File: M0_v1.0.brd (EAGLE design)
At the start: 68.6 x 53.3 mm, 54 parts, among them CN1 POWER_JACK, CN2 47346-0001, CN3 DIGITAL10, CN4 DIGITAL8, CN5 ICSP, CN6 POWER8, CN7 ANALOG6, IC1 AMS1117-5.0, IC2 AMS1117-3.3, IC3 MCP6002T-I/SN, Q2 16MHz, T1 AO3401A, T2 2N7002, U1 ATSAMD21G-A

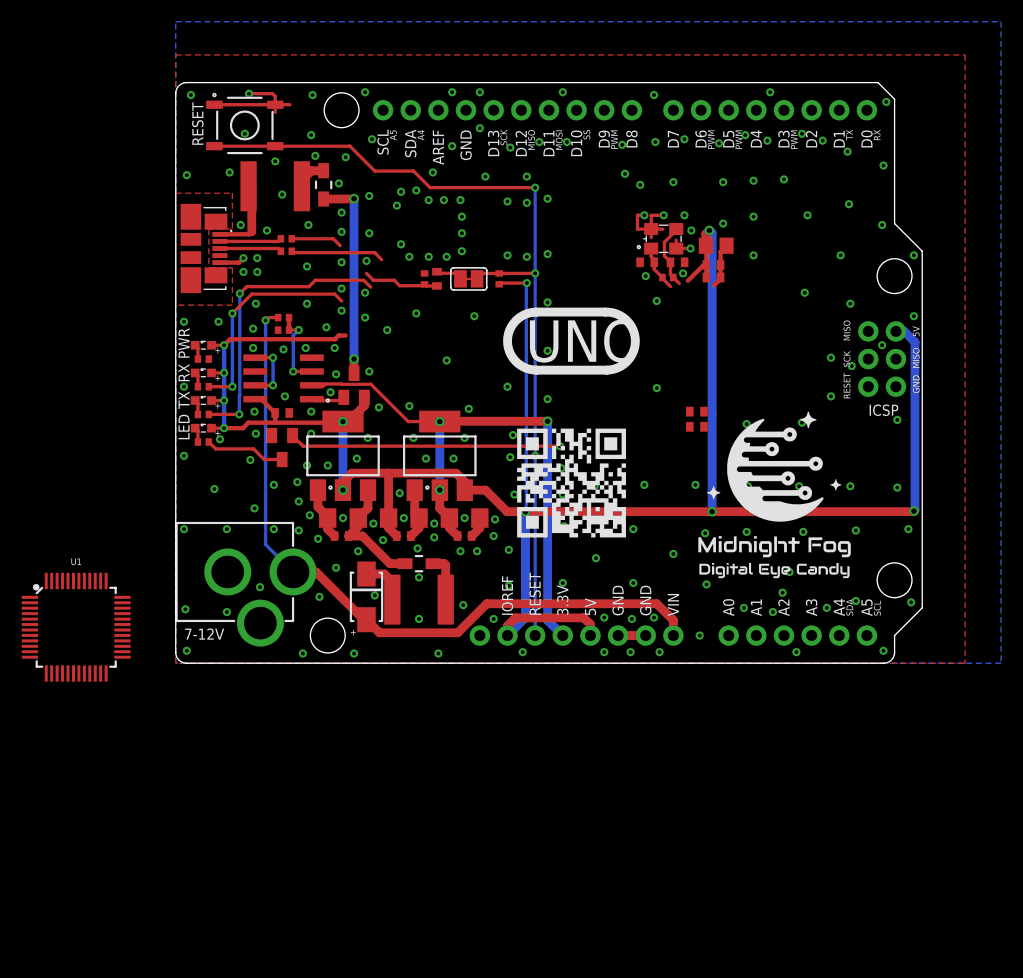
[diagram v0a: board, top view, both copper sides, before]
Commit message: Add basic signal wiring.
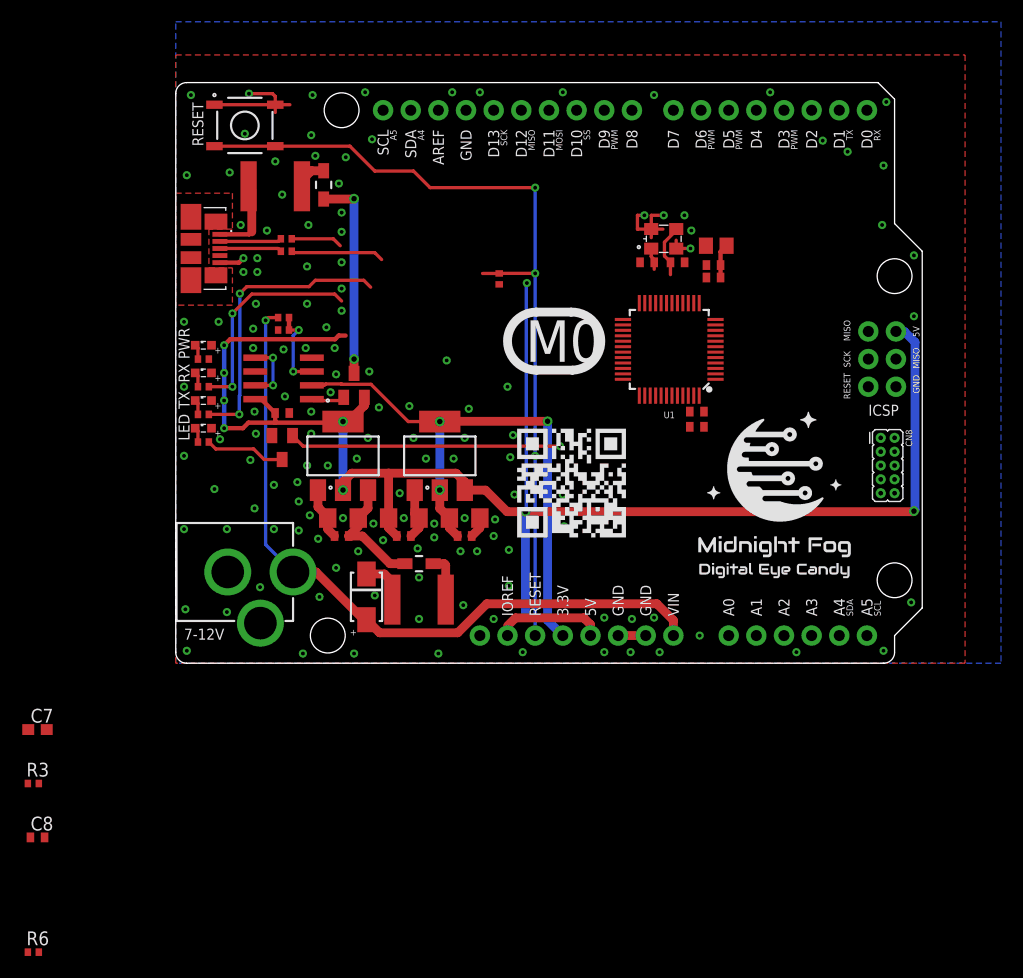
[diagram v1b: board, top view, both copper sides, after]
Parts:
- removed C18: 100nF, rcl:C0402
- removed R11: 1K, rcl:R0402
- removed SJ1: USB_RESET, _my_jumpers:SJ
- added C7: 1uF, rcl:C0603
- added C8: 10nF, rcl:C0402
- added CN8: SWD, SparkFun-Connectors:2X5_PTH_SILK_.05
- added R3: 330R, rcl:R0402
- Q2: value 16MHz -> 32.768KHz
- R10, R7, R8, R9: value 1K -> 470R
- R6: value 1M -> 330R
- U1: value ATSAMD21G-A -> ATSAMD21G-AU
- moved R6 85.1 mm to (-13.1, -26.5)
- moved U1 60.2 mm to (45.3, 28.8), turned to 180 degrees
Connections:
- removed net A4_SDA: CN3.2, CN7.2
- removed net A5_SCL: CN3.1, CN7.1
- removed net MCU_OSC_IN: C12.2, Q2.3, R6.2
- removed net MCU_OSC_OUT: C13.2, Q2.1, R6.1
- removed net N$5: C18.2, SJ1.1
- removed net USB_DTR: C18.1, R11.2
- new net A4: CN7.2, U1.10
- new net A5: CN7.1, U1.47
- new net MCU_OSC32_IN: C12.2, Q2.3, U1.1
- new net MCU_OSC32_OUT: C13.2, Q2.1, U1.2
- new net MCU_RESET: C8.1, R3.1, U1.40
- new net N$20: U1.48
- new net N$28: U1.22
- new net N$41: U1.39
- new net N$47: U1.37
- new net N$48: U1.38
- new net N$6: U1.4
- new net SCL: CN3.1, U1.32
- new net SDA: CN3.2, U1.31
- new net SPI_MISO: CN5.1, U1.21
- new net SPI_MOSI: CN5.4, U1.19
- new net SPI_SCK: CN5.3, U1.20
- new net SWDCLK: CN8.3, U1.45
- new net SWDIO: CN8.1, U1.46
- new net USB_EN: R6.2, U1.41
- new net VDDANA: U1.6
- new net VDDCORE: C7.1, U1.43
- new net XUSB_EN: CN2.4, R6.1
- net 3.3V: now also C14.1, C15.1, C16.1, C17.1, CN6.7, LED1.A, LED2.A, LED3.A, LED4.A, R12.2, U1.17, U1.36, U1.44
- net 5V: now also CN8.2; no longer C14.1, C15.1, C16.1, C17.1, CN6.7, LED1.A, LED2.A, LED3.A, LED4.A, R12.2
- net A0: now also U1.3
- net A1: now also U1.7
- net A2: now also U1.8
- net A3: now also U1.9
- net D0_RX: now also U1.16
- net D10_SS: now also U1.27
- net D11_MOSI: now also U1.25; no longer CN5.4
- net D12_MISO: now also U1.28; no longer CN5.1
- net D13_SCK: now also U1.26; no longer CN5.3
- net D1_TX: now also U1.15
- net D2: now also U1.23
- net D3_PWM: now also U1.14
- net D4: now also U1.13
- net D5_PWM: now also U1.24
- net D6_PWM: now also U1.29
- net D7: now also U1.30
- net D8: now also U1.11
- net D9_PWM: now also U1.12
- net GND: now also C7.2, C8.2, CN8.10, CN8.4, CN8.6, U1.18, U1.35, U1.42, U1.5; no longer R11.1
- net RESET: now also CN8.9, R3.2; no longer SJ1.2
- net USB_D_M: now also U1.33
- net USB_D_P: now also U1.34
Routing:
- net 5V: track 205.8 -> 162.4 mm, vias 11 -> 9
- net USB_DTR: track 7.06 -> 0.00 mm
- net MCU_OSC_IN: track 6.02 -> 0.00 mm
- net MCU_OSC32_IN: track 0.00 -> 4.87 mm
- net MCU_OSC_OUT: track 4.22 -> 0.00 mm
- net N$5: track 2.43 -> 0.00 mm
- net MCU_OSC32_OUT: track 0.00 -> 2.02 mm
- net RESET: track 78.8 -> 77.0 mm
- net GND: track 40.9 -> 40.1 mm, vias 232 -> 137
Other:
- board text added: "M0"
- board text removed: "UNO"

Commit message: Add proper power selection. Move stuff around.
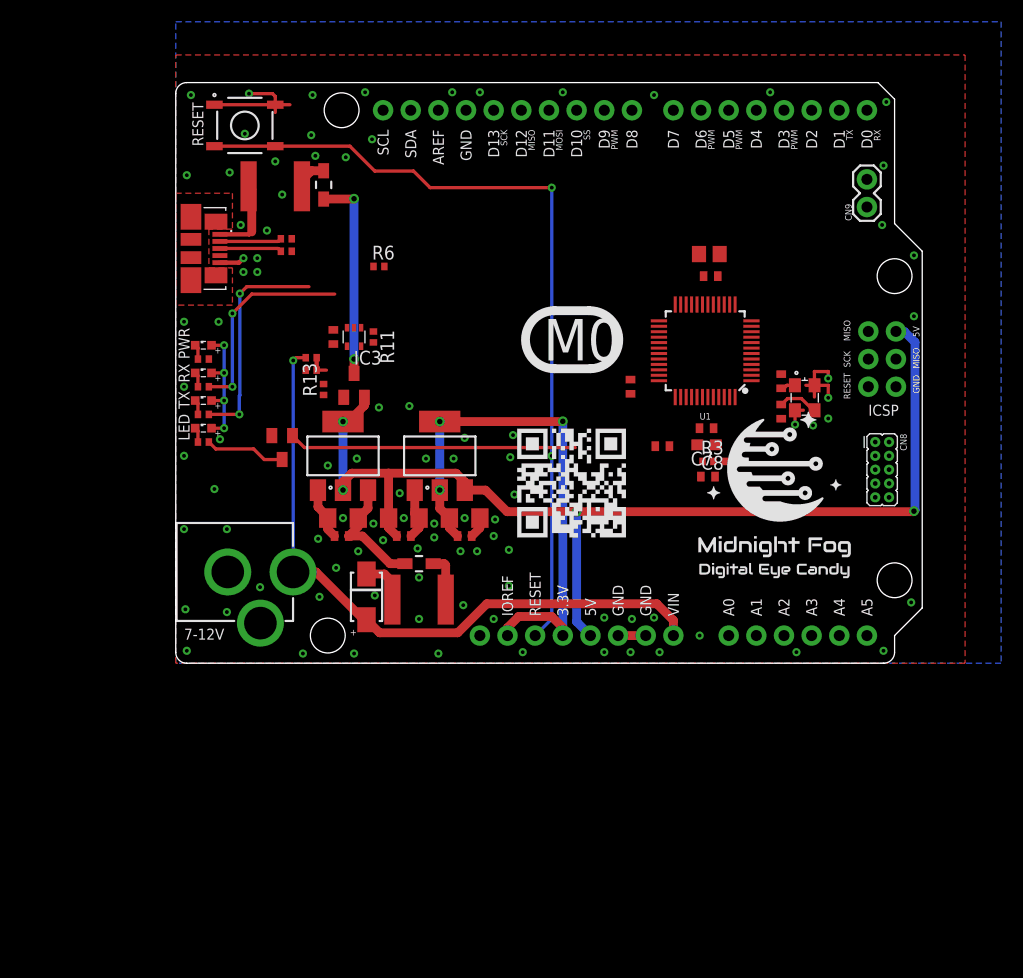
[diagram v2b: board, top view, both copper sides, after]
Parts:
- added CN9: UART, SparkFun-Connectors:1X02
- added R11: 100K, rcl:R0402
- added R13: 47K, rcl:R0402
- IC3: value MCP6002T-I/SN -> 74LVC1G125DCK; device linear:SO08 -> 74xx-little-us:SC70-5
- R5: value 100K -> 47K
- moved R6 70.5 mm to (18.7, 36.4)
- moved C8 69.9 mm to (48.9, 17.1)
- moved R3 68.7 mm to (48.9, 18.5)
- moved C7 66.8 mm to (48.8, 20.1), turned to 180 degrees
- moved R12 27.0 mm to (50.9, 18.5), turned to 0 degrees
- moved Q2 19.5 mm to (57.8, 24.4), turned to 270 degrees
- moved C12 16.7 mm to (55.6, 23.1), turned to 90 degrees
- moved C13 16.5 mm to (55.6, 25.9), turned to 270 degrees
- moved C14 13.5 mm to (41.8, 25.4), turned to 90 degrees
- moved C11 8.42 mm to (14.5, 30.0), turned to 90 degrees
- moved IC3 7.51 mm to (16.4, 30.0), turned to 180 degrees
- moved R4 4.47 mm to (12.4, 28.1)
- moved R5 4.47 mm to (12.4, 26.9)
- moved C19 3.64 mm to (44.7, 19.9), turned to 180 degrees
- moved U1 3.30 mm to (48.6, 28.7)
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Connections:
- removed net N$1: IC3.5, IC3.7
- removed net N$47: U1.37
- removed net N$48: U1.38
- removed net N$6: U1.4
- removed net N$8: IC3.1, T1.1
- new net UART_RX: CN9.2, U1.38
- new net UART_TX: CN9.1, U1.37
- net 3.3V: now also C11.1, IC3.5, R11.2; no longer IC3.2
- net 5V: now also R13.1; no longer C11.1, IC3.8
- net AREF: now also U1.4
- net GND: now also IC3.3; no longer IC3.4, IC3.6
- net N$12: now also IC3.4, R13.2, T1.1; no longer IC3.3
- net XUSB_EN: now also IC3.1, IC3.2, R11.1
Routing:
- net 5V: track 162.4 -> 101.1 mm, vias 9 -> 4
- net USB_D_P: track 8.57 -> 0.18 mm
- net D1_TX: track 26.7 -> 20.5 mm
- net 3.3V: track 55.7 -> 61.8 mm, vias 3 -> 7
- net N$1: track 5.81 -> 0.00 mm, vias 2 -> 0
- net N$12: track 7.77 -> 2.04 mm, vias 2 -> 0
- net VIN: track 65.8 -> 61.1 mm
- net USB_D_M: track 4.72 -> 0.00 mm
- net GND: track 40.1 -> 36.8 mm, vias 137 -> 94
- net N$8: track 3.10 -> 0.00 mm
- net RESET: track 77.0 -> 74.3 mm, vias 3 -> 2
- net D13_SCK: track 25.0 -> 26.4 mm, vias 1 -> 0
- net MCU_OSC32_IN: track 4.87 -> 3.74 mm
- net D0_RX: track 20.1 -> 19.2 mm
- net MCU_OSC32_OUT: track 2.02 -> 1.37 mm
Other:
- board text added: "M0 v1.0 (c) Andriy Golovnya Designed in Germany http://redscorp.net"
- board text removed: "UNO v1.0 (c) Andriy Golovnya Designed in Germany http://redscorp.net"

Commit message: Add second MCU footprint. Add some wires. Routed the board for now.
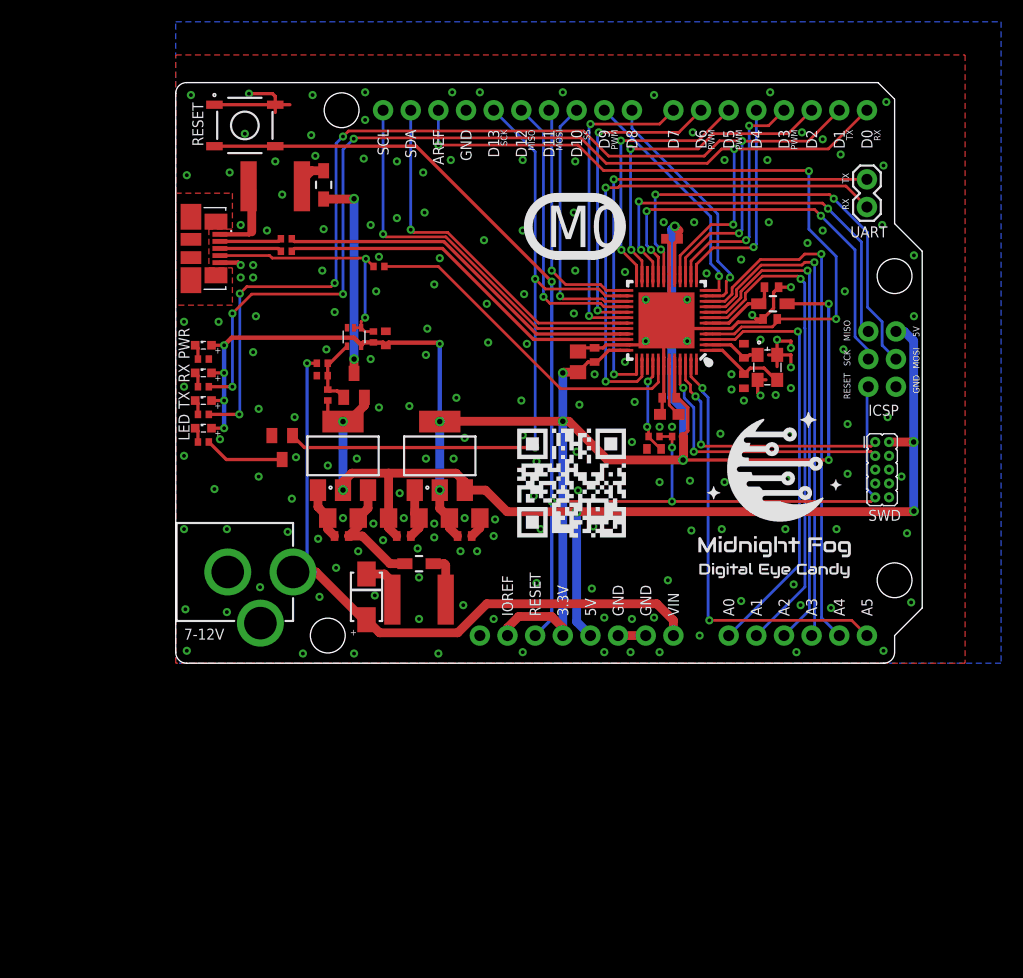
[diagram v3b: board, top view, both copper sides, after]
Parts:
- added C9: 100nF, rcl:C0402
- added L3: GZ2012D601TF, Wurth_Automotive_WE-CBA:WE-CBA_0805(W=4)
- added U2: ATSAMD21G-MU, SparkFun-IC-Microcontroller:QFN-48
- moved C17 15.6 mm to (37.0, 27.7), turned to 90 degrees
- moved C19 15.3 mm to (54.6, 31.6)
- moved C8 5.57 mm to (43.9, 19.7), turned to 180 degrees
- moved R3 5.46 mm to (43.9, 20.8)
- moved R12 5.34 mm to (46.1, 20.8)
- moved C15 4.94 mm to (45.6, 39.0)
- moved C11 4.83 mm to (19.3, 29.8)
- moved U1 4.52 mm to (45.1, 31.5)
- moved C16 4.42 mm to (45.3, 24.4)
- moved C7 4.42 mm to (45.3, 22.9)
- moved C12 4.42 mm to (52.2, 25.9)
- moved C13 4.42 mm to (52.2, 28.7)
- moved Q2 4.42 mm to (54.4, 27.2)
- moved C14 4.41 mm to (38.5, 28.3)
- moved CN9 2.54 mm to (63.5, 44.5), turned to 270 degrees
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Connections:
- removed net N$20: U1.48
- removed net N$28: U1.22
- removed net N$41: U1.39
- net 3.3V: now also L3.2, U2.17, U2.36, U2.44
- net A0: now also U2.3
- net A1: now also U2.7
- net A2: now also U2.8
- net A3: now also U2.9
- net A4: now also U2.10
- net A5: now also U2.47
- net AREF: now also U2.4
- net D0_RX: now also U2.16
- net D10_SS: now also U2.27
- net D11_MOSI: now also U2.25
- net D12_MISO: now also U2.28
- net D13_SCK: now also U2.26
- net D1_TX: now also U2.15
- net D2: now also U2.23
- net D3_PWM: now also U2.14
- net D4: now also U2.13
- net D5_PWM: now also U2.24
- net D6_PWM: now also U2.29
- net D7: now also U2.30
- net D8: now also U2.11
- net D9_PWM: now also U2.12
- net GND: now also C9.2, U2.18, U2.35, U2.42, U2.5
- net MCU_OSC32_IN: now also U2.1
- net MCU_OSC32_OUT: now also U2.2
- net MCU_RESET: now also U2.40
- net SCL: now also U2.32
- net SDA: now also U2.31
- net SPI_MISO: now also U2.21
- net SPI_MOSI: now also U2.19
- net SPI_SCK: now also U2.20
- net SWDCLK: now also U2.45
- net SWDIO: now also U2.46
- net UART_RX: now also U2.38
- net UART_TX: now also U2.37
- net USB_D_M: now also U2.33
- net USB_D_P: now also U2.34
- net USB_EN: now also U2.41
- net VDDANA: now also C9.1, L3.1, U2.6
- net VDDCORE: now also U2.43
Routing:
- net 3.3V: track 61.8 -> 183.2 mm, vias 7 -> 13
- net D1_TX: track 20.5 -> 102.1 mm, vias 2 -> 6
- net D0_RX: track 19.2 -> 100.2 mm, vias 2 -> 6
- net AREF: track 0.00 -> 65.8 mm, vias 0 -> 3
- net A4: track 0.00 -> 48.7 mm, vias 0 -> 1
- net UART_RX: track 0.00 -> 48.0 mm, vias 0 -> 2
- net A3: track 0.00 -> 46.7 mm, vias 0 -> 1
- net A2: track 0.00 -> 46.1 mm, vias 0 -> 1
- net A1: track 0.00 -> 45.7 mm, vias 0 -> 1
- net UART_TX: track 0.00 -> 44.8 mm, vias 0 -> 2
- net RESET: track 74.3 -> 116.8 mm, vias 2 -> 4
- net SPI_MOSI: track 0.00 -> 42.1 mm, vias 0 -> 3
- net A5: track 0.00 -> 39.9 mm, vias 0 -> 2
- net A0: track 0.72 -> 39.7 mm, vias 0 -> 1
- net SPI_MISO: track 0.00 -> 38.5 mm, vias 0 -> 3
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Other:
- board text added: "SWD"
- board text added: "UART"
